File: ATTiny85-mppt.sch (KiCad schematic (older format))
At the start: 51 parts, among them J1 S+, J2 S-, J3 O+, J4 O-, Q1 BUK9511-55A127, Q2 BUK9511-55A127, Q3 2N2222A, Q4 2N2222A, Q5 2N2907A, Q6 2N2222A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

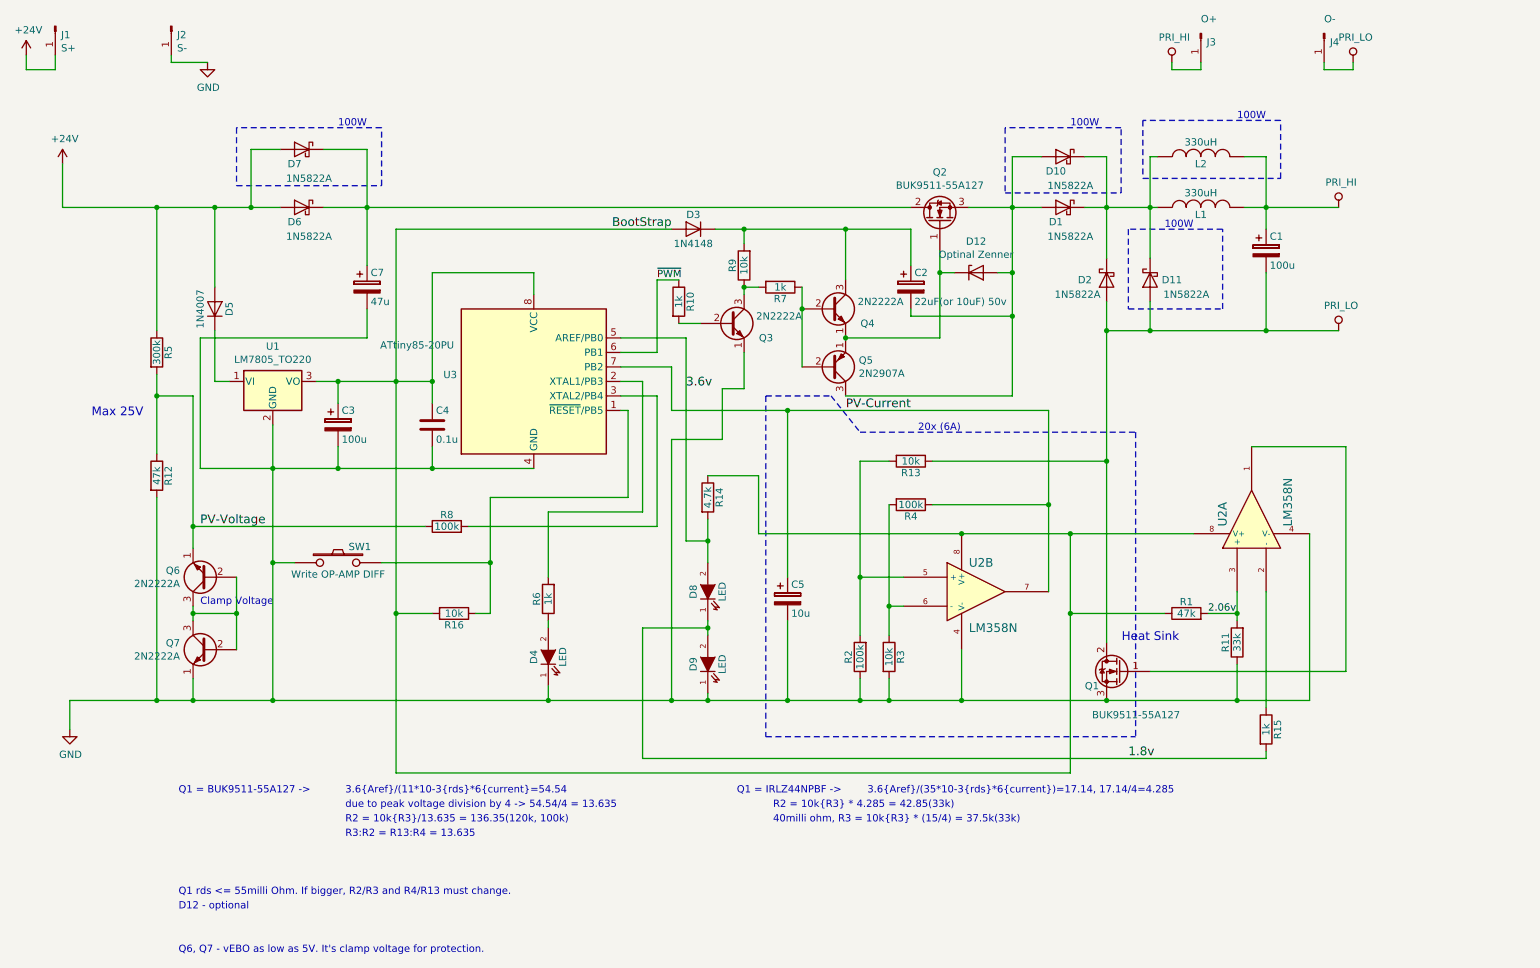
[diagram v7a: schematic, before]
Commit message: Back to old circuit. Fix power-up high-z on at FET.
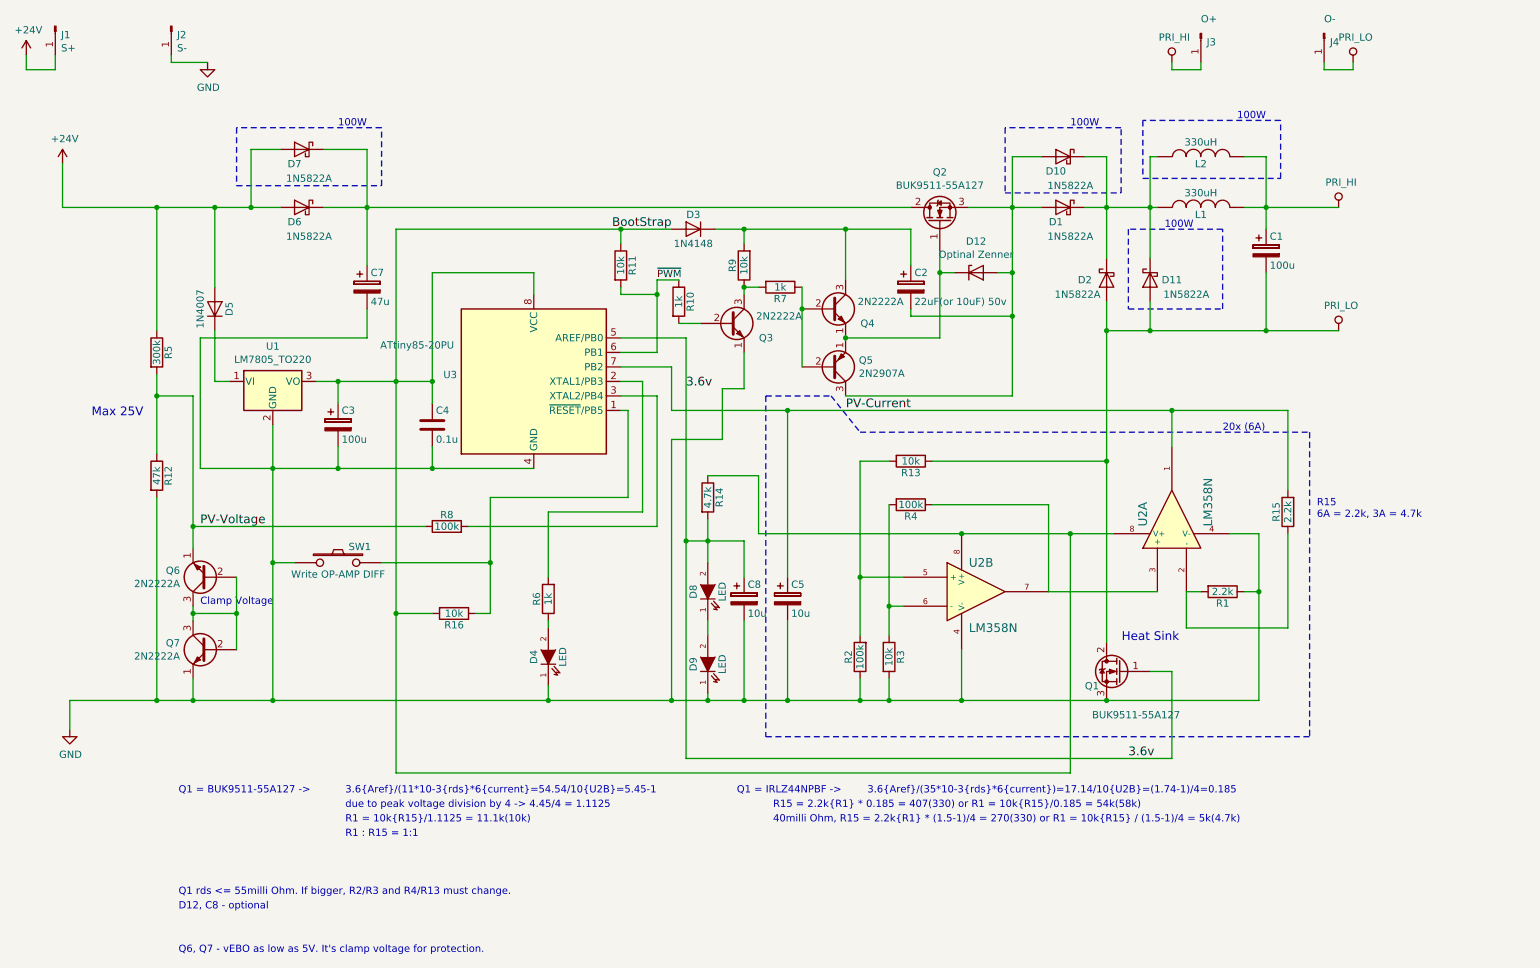
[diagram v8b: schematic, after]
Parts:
- added C8: 10u, Capacitors_THT:CP_Radial_D12.5mm_P5.00mm, symbol Device:CP
- R1: value 47k -> 2.2k
- R11: value 33k -> 10k
- R15: value 1k -> 2.2k
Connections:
- net 3.6v: now also Q1.1 (G), C8.1
- net BootStrap: now also R11.1; no longer R1.1
- net GND: now also R1.1, C8.2; no longer R11.1
- net PV-Current: now also R15.2, U2.1; no longer R4.1, U2.7
- net ~PWM: now also R11.2
- net at R15.1, U2.2 (-): now also R1.2
- net 1.8v: no longer names the net of D8.1 (K), D9.2 (A)
- net 1.8v: no longer R15.2
- removed net 2.06v: R1.2, R11.2, U2.3 (+)
- new net: R4.1, U2.3 (+), U2.7
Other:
- note added: "3.6{Aref}/(11*10-3{rds}*6{current}=54.54/10{U2B}=5.45-1"
- note added: "3.6{Aref}/(35*10-3{rds}*6{current})=17.14/10{U2B}=(1.74-1)/4=0.185"
- note added: "40milli Ohm, R15 = 2.2k{R1} * (1.5-1)/4 = 270(330) or R1 = 10k{R15} / (1.5-1)/4 = 5k(4.7k)"
- note added: "D12, C8 - optional"
- note added: "R1 : R15 = 1:1"
- note added: "R1 = 10k{R15}/1.1125 = 11.1k(10k)"
- note added: "R15 = 2.2k{R1} * 0.185 = 407(330) or R1 = 10k{R15}/0.185 = 54k(58k)"
- note added: "R15\n6A = 2.2k, 3A = 4.7k"
- note added: "due to peak voltage division by 4 -> 4.45/4 = 1.1125"
- note removed: "3.6{Aref}/(11*10-3{rds}*6{current}=54.54"
- note removed: "3.6{Aref}/(35*10-3{rds}*6{current})=17.14, 17.14/4=4.285"
- note removed: "40milli ohm, R3 = 10k{R3} * (15/4) = 37.5k(33k)"
- note removed: "D12 - optional"
- note removed: "R2 = 10k{R3} * 4.285 = 42.85(33k)"
- note removed: "R2 = 10k{R3}/13.635 = 136.35(120k, 100k)"
- note removed: "R3:R2 = R13:R4 = 13.635"
- note removed: "due to peak voltage division by 4 -> 54.54/4 = 13.635"
- moved on the sheet: R1, R15, U2A
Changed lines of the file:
@@
 Sheet 1 1
 Title "Simple MPPT with ATTiny85"
-Date "2019-02-09"
-Rev "2.1"
+Date "2019-02-13"
+Rev "1.92"
 Comp ""
 Comment1 ""
@@
 $EndComp
 Text Label 8550 6000 0    60   ~ 0
-1.8v
+3.6v
+$Comp
+L ATTiny85-mppt-rescue:LM358N-RESCUE-12f675-mppt-12f675-mppt-rescue U2
+U 1 1 56E669E2
+P 8850 4350
+F 0 "U2" H 8800 4550 60  0000 L CNN
+F 1 "LM358N" H 8800 4100 60  0000 L CNN
+F 2 "Housings_DIP:DIP-8_W7.62mm" H 8850 4350 60  0001 C CNN
+F 3 "" H 8850 4350 60  0000 C CNN
+	1    8850 4350
+	0    -1   -1   0
+$EndComp
 $Comp
 L Device:R R1
 U 1 1 56E67518
-P 8950 5000
-F 0 "R1" V 9030 5000 50  0000 C CNN
-F 1 "47k" V 8950 5000 50  0000 C CNN
-F 2 "Resistors_THT:R_Axial_DIN0309_L9.0mm_D3.2mm_P12.70mm_Horizontal" V 8880 5000 50  0001 C CNN
-F 3 "" H 8950 5000 50  0000 C CNN
-	1    8950 5000
-	0    -1   -1   0
+P 9200 4850
+F 0 "R1" V 9280 4850 50  0000 C CNN
+F 1 "2.2k" V 9200 4850 50  0000 C CNN
+F 2 "Resistors_THT:R_Axial_DIN0309_L9.0mm_D3.2mm_P12.70mm_Horizontal" V 9130 4850 50  0001 C CNN
+F 3 "" H 9200 4850 50  0000 C CNN
+	1    9200 4850
+	0    1    1    0
 $EndComp
 $Comp
 L Device:R R15
 U 1 1 56E68956
-P 9500 5800
-F 0 "R15" V 9580 5800 50  0000 C CNN
-F 1 "1k" V 9500 5800 50  0000 C CNN
-F 2 "Resistors_THT:R_Axial_DIN0309_L9.0mm_D3.2mm_P12.70mm_Horizontal" V 9430 5800 50  0001 C CNN
-F 3 "" H 9500 5800 50  0000 C CNN
-	1    9500 5800
-	1    0    0    -1
+P 9650 4300
+F 0 "R15" V 9730 4300 50  0000 C CNN
+F 1 "2.2k" V 9650 4300 50  0000 C CNN
+F 2 "Resistors_THT:R_Axial_DIN0309_L9.0mm_D3.2mm_P12.70mm_Horizontal" V 9580 4300 50  0001 C CNN
+F 3 "" H 9650 4300 50  0000 C CNN
+	1    9650 4300
+	-1   0    0    1
 $EndComp
 Wire Wire Line
@@
 Connection ~ 7750 2200
 Wire Wire Line
-	5400 2350 3500 2350
+	5400 2350 5050 2350
 Connection ~ 2250 2200
 Connection ~ 2650 5600
@@
 Connection ~ 9500 2200
 Wire Notes Line
-	6050 5850 8600 5850
+	6050 5850 9800 5850
 Wire Wire Line
 	1850 4200 1850 5600
@@
 	5650 4350 5650 4500
 Wire Wire Line
-	5650 5050 5650 5100
+	5650 5050 5650 5150
 Wire Wire Line
 	5650 5550 5650 5600
@@
 Wire Wire Line
 	6200 4750 6200 3600
+Connection ~ 6200 3600
 Wire Notes Line
 	6050 3500 6050 5850
@@
 	6500 3500 6700 3750
 Wire Notes Line
-	6700 3750 8600 3750
+	6700 3750 9800 3750
 Wire Wire Line
 	3500 6100 8150 6100
+Wire Wire Line
+	8150 6100 8150 4450
 Wire Wire Line
 	4550 4300 4550 4750
@@
 	6000 4050 6000 4450
 Wire Wire Line
+	8850 5400 8700 5400
+Wire Wire Line
+	5500 6000 8850 6000
+Wire Wire Line
+	8850 6000 8850 5400
+Connection ~ 5500 4500
+Wire Wire Line
 	6000 4450 7400 4450
 Wire Wire Line
-	9800 5600 9300 5600
+	9450 5600 8400 5600
 Wire Wire Line
 	8000 4250 8000 4850
+Wire Wire Line
+	8000 4850 8750 4850
+Wire Wire Line
+	8850 3850 8850 3600
+Wire Wire Line
+	9450 4450 9450 4850
 Connection ~ 8400 5600
+Wire Wire Line
+	9050 4850 8950 4850
+Wire Wire Line
+	9450 4450 9250 4450
+Connection ~ 9450 4850
 Connection ~ 8150 4450
-Wire Notes Line
-	8600 3750 8600 5850
+Wire Wire Line
+	9650 5100 9650 4450
+Wire Wire Line
+	9650 3600 9650 4150
+Connection ~ 8850 3600
+Wire Notes Line
+	9800 3750 9800 5850
+Wire Wire Line
+	9350 4850 9450 4850
+Wire Wire Line
+	9650 5100 8950 5100
+Wire Wire Line
+	8950 5100 8950 4850
 $Comp
 L Device:CP C7
@@
 	5650 4500 5650 4650
 Wire Wire Line
+	5500 4500 5500 6000
+Wire Wire Line
 	8400 5600 7400 5600
 Wire Wire Line
-	8150 4450 9000 4450
+	9450 4850 9450 5600
+Wire Wire Line
+	8150 4450 8450 4450
+Wire Wire Line
+	8850 3600 9650 3600
 Wire Wire Line
 	3300 2200 3000 2200
@@
 Wire Wire Line
 	5200 3400 5050 3400
+Wire Wire Line
+	5650 5600 5900 5600
 Wire Wire Line
 	5500 3100 5500 4500
@@
 Wire Notes Line
 	9200 2350 8550 2350
-Text Notes 7100 3750 0    50   ~ 0
+Text Notes 9200 3750 0    50   ~ 0
 20x (6A)
 Text Notes 3100 1650 0    50   ~ 0
@@
 Q1 = IRLZ44NPBF ->
 Text Notes 6750 6250 0    50   ~ 0
-3.6{Aref}/(35*10-3{rds}*6{current})=17.14, 17.14/4=4.285
+3.6{Aref}/(35*10-3{rds}*6{current})=17.14/10{U2B}=(1.74-1)/4=0.185
 Text Notes 6100 6350 0    50   ~ 0
-R2 = 10k{R3} * 4.285 = 42.85(33k)
+R15 = 2.2k{R1} * 0.185 = 407(330) or R1 = 10k{R15}/0.185 = 54k(58k)
 Text Notes 2000 6250 0    50   ~ 0
 Q1 = BUK9511-55A127 ->
 Text Notes 3150 6250 0    50   ~ 0
-3.6{Aref}/(11*10-3{rds}*6{current}=54.54
+3.6{Aref}/(11*10-3{rds}*6{current}=54.54/10{U2B}=5.45-1
 Text Notes 3150 6450 0    50   ~ 0
-R2 = 10k{R3}/13.635 = 136.35(120k, 100k)
+R1 = 10k{R15}/1.1125 = 11.1k(10k)
 Text Notes 6100 6450 0    50   ~ 0
-40milli ohm, R3 = 10k{R3} * (15/4) = 37.5k(33k)
+40milli Ohm, R15 = 2.2k{R1} * (1.5-1)/4 = 270(330) or R1 = 10k{R15} / (1.5-1)/4 = 5k(4.7k)
 Text Notes 2000 6950 0    50   ~ 0
 Q1 rds <= 55milli Ohm. If bigger, R2/R3 and R4/R13 must change.
@@
 $EndComp
 Wire Wire Line
-	5300 3200 5300 2700
+	5300 3200 5300 2800
 Wire Wire Line
 	5300 2700 5450 2700
 Wire Wire Line
 	5450 3000 5600 3000
+$Comp
+L Device:CP C8
+U 1 1 5BE62CB0
+P 5900 4900
+F 0 "C8" H 5925 5000 50  0000 L CNN
+F 1 "10u" H 5925 4800 50  0000 L CNN
+F 2 "Capacitors_THT:CP_Radial_D12.5mm_P5.00mm" H 5938 4750 30  0001 C CNN
+F 3 "" H 5900 4900 60  0000 C CNN
+	1    5900 4900
+	1    0    0    -1
+$EndComp
+Wire Wire Line
+	5900 4750 5900 4500
+Wire Wire Line
+	5900 4500 5650 4500
+Wire Wire Line
+	5900 5050 5900 5600
+Connection ~ 5900 5600
+Wire Wire Line
+	5900 5600 6200 5600
 $Comp
 L Device:D_Zener D12
@@
 	5050 3100 5500 3100
 Wire Wire Line
+	6200 3600 8850 3600
+Wire Wire Line
 	6600 3100 7250 3100
 Text Notes 2000 7050 0    50   ~ 0
-D12 - optional
+D12, C8 - optional
 Wire Wire Line
 	2650 5600 4550 5600
@@
 	4000 4400 5300 4400
 Text Notes 3150 6350 0    50   ~ 0
-due to peak voltage division by 4 -> 54.54/4 = 13.635
+due to peak voltage division by 4 -> 4.45/4 = 1.1125
 Text Notes 3150 6550 0    50   ~ 0
-R3:R2 = R13:R4 = 13.635
+R1 : R15 = 1:1
+Text Notes 9850 4350 0    50   ~ 0
+R15\n6A = 2.2k, 3A = 4.7k
 $Comp
 L Device:Q_NPN_EBC Q6
@@
 Text Notes 2000 7350 0    50   ~ 0
 Q6, Q7 - vEBO as low as 5V. It's clamp voltage for protection.
-Wire Wire Line
-	8000 4250 8000 3600
-Wire Wire Line
-	8000 3600 6200 3600
-Connection ~ 8000 4250
-Connection ~ 6200 3600
-Wire Wire Line
-	9800 4450 9800 5600
-$Comp
-L ATTiny85-mppt-rescue:LM358N-RESCUE-12f675-mppt-12f675-mppt-rescue U2
-U 1 1 56E669E2
-P 9400 4350
-F 0 "U2" H 9350 4550 60  0000 L CNN
-F 1 "LM358N" H 9350 4100 60  0000 L CNN
-F 2 "Housings_DIP:DIP-8_W7.62mm" H 9400 4350 60  0001 C CNN
-F 3 "" H 9400 4350 60  0000 C CNN
-	1    9400 4350
-	0    -1   -1   0
-$EndComp
-Wire Wire Line
-	9400 3850 10050 3850
-Wire Wire Line
-	10050 3850 10050 5400
-Wire Wire Line
-	10050 5400 8700 5400
-Wire Wire Line
-	8150 4450 8150 5000
-Wire Wire Line
-	8800 5000 8150 5000
-Connection ~ 8150 5000
-Wire Wire Line
-	8150 5000 8150 6100
-Wire Wire Line
-	9300 4850 9300 5000
-Wire Wire Line
-	9100 5000 9300 5000
-Wire Wire Line
-	5650 5100 5200 5100
-Wire Wire Line
-	5200 5100 5200 6000
-Wire Wire Line
-	5200 6000 9500 6000
-Wire Wire Line
-	9500 6000 9500 5950
-Connection ~ 5650 5100
-Wire Wire Line
-	5650 5100 5650 5150
-Wire Wire Line
-	9500 4850 9500 5650
 $Comp
 L Device:R R11
-U 1 1 5C6A7369
-P 9300 5200
-F 0 "R11" V 9380 5200 50  0000 C CNN
-F 1 "33k" V 9300 5200 50  0000 C CNN
-F 2 "Resistors_THT:R_Axial_DIN0309_L9.0mm_D3.2mm_P12.70mm_Horizontal" V 9230 5200 50  0001 C CNN
-F 3 "" H 9300 5200 50  0000 C CNN
-	1    9300 5200
-	-1   0    0    1
-$EndComp
-Wire Wire Line
-	9300 5000 9300 5050
-Connection ~ 9300 5000
-Wire Wire Line
-	9300 5350 9300 5600
-Connection ~ 9300 5600
-Wire Wire Line
-	9300 5600 8400 5600
-Text Label 9100 5000 0    50   ~ 0
-2.06v
-Wire Wire Line
-	5650 5600 6200 5600
+U 1 1 5C645AD6
+P 5050 2600
+F 0 "R11" V 5130 2600 50  0000 C CNN
+F 1 "10k" V 5050 2600 50  0000 C CNN
+F 2 "Resistors_THT:R_Axial_DIN0309_L9.0mm_D3.2mm_P12.70mm_Horizontal" V 4980 2600 30  0001 C CNN
+F 3 "" H 5050 2600 30  0000 C CNN
+	1    5050 2600
+	1    0    0    -1
+$EndComp
+Wire Wire Line
+	5050 2750 5050 2800
+Wire Wire Line
+	5050 2800 5300 2800
+Connection ~ 5300 2800
+Wire Wire Line
+	5300 2800 5300 2700
+Wire Wire Line
+	5050 2450 5050 2350
+Connection ~ 5050 2350
+Wire Wire Line
+	5050 2350 3500 2350
 $EndSCHEMATC
